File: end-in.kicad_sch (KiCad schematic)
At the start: 4 parts

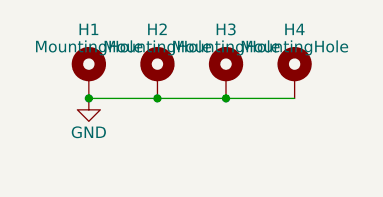
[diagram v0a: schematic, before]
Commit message: Use a plated hole for the LED panel opening
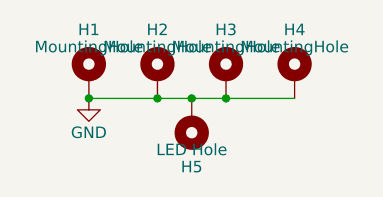
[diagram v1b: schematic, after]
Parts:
- added H5: LED Hole, Parts:LED_Hole, symbol Mechanical:MountingHole_Pad
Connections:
- net GND: now also H5.1
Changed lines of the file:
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@@
+	)
+	(junction
+		(at 87.63 67.31)
+		(diameter 0)
+		(color 0 0 0 0)
 	)
 	(junction
@@
 	(wire
 		(pts
+			(xy 87.63 67.31) (xy 91.44 67.31)
+		)
+		(stroke
+			(width 0)
+			(type default)
+		)
+	)
+	(wire
+		(pts
 			(xy 76.2 67.31) (xy 83.82 67.31)
 		)
@@
 	(wire
 		(pts
-			(xy 83.82 67.31) (xy 91.44 67.31)
+			(xy 83.82 67.31) (xy 87.63 67.31)
 		)
 		(stroke
@@
 					(unit 1)
 				)
+			)
+		)
+	)
+	(symbol
+		(lib_id "Mechanical:MountingHole_Pad")
+		(at 87.63 69.85 180)
+		(unit 1)
+		(exclude_from_sim no)
+		(in_bom no)
+		(on_board yes)
+		(dnp no)
+		(property "Reference" "H5"
+			(at 87.63 74.93 0)
+			(effects
+				(font
+					(size 1.27 1.27)
+				)
+			)
+		)
+		(property "Value" "LED Hole"
+			(at 87.63 73.025 0)
+			(effects
+				(font
+					(size 1.27 1.27)
+				)
+			)
+		)
+		(property "Footprint" "Parts:LED_Hole"
+			(at 87.63 69.85 0)
+			(effects
+				(font
+					(size 1.27 1.27)
+				)
+				(hide yes)
+			)
+		)
+		(property "Datasheet" "~"
+			(at 87.63 69.85 0)
+			(effects
+				(font
+					(size 1.27 1.27)
+				)
+				(hide yes)
+			)
+		)
+		(property "Description" "Mounting Hole with connection"
+			(at 87.63 69.85 0)
+			(effects
+				(font
+					(size 1.27 1.27)
+				)
+				(hide yes)
+			)
+		)
+		(property "JLCPCB" ""
+			(at 87.63 69.85 0)
+			(effects
+				(font
+					(size 1.27 1.27)
+				)
+				(hide yes)
+			)
+		)
+		(pin "1"
+		)
+		(instances
+			(project "end-in"
+				(path "/7c517696-5291-4036-b4fd-2220f5916b7c"
+					(reference "H5")
+					(unit 1)
+				)
